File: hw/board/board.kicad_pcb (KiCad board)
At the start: 4 copper layers, 100 x 85 mm, 77 parts, among them J1 Conn_ARM_JTAG_SWD_10, J2 Conn_ARM_JTAG_SWD_10, SW1 TSB008A2526A, SW2 TSB008A2526A, U1 STM32F302CBTx, U2 W25Q128JVSIQTR, U3 AP7361C-18SP-13, U4 AP7361C-10E, U5 TPS54331DR, U6 XC7A35T-FTG256

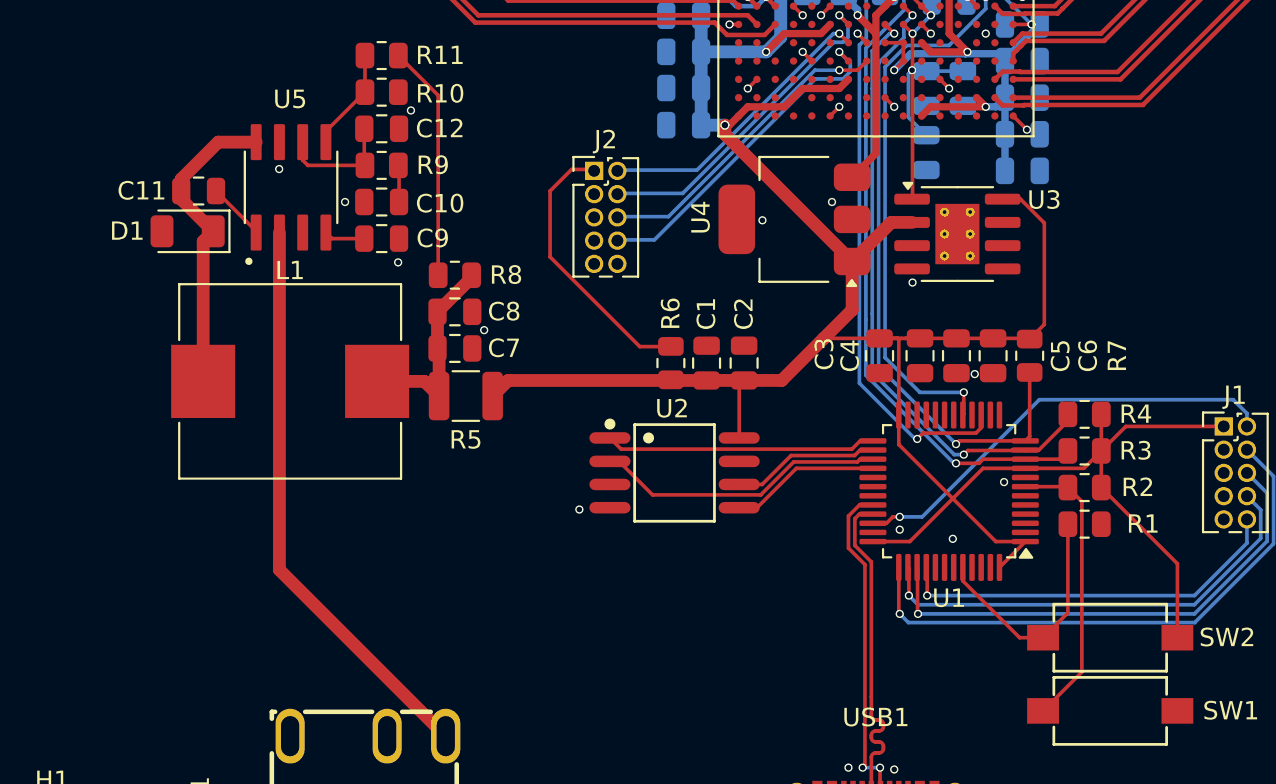
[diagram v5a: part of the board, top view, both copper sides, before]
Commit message: Added capacitor for STM32 NRST
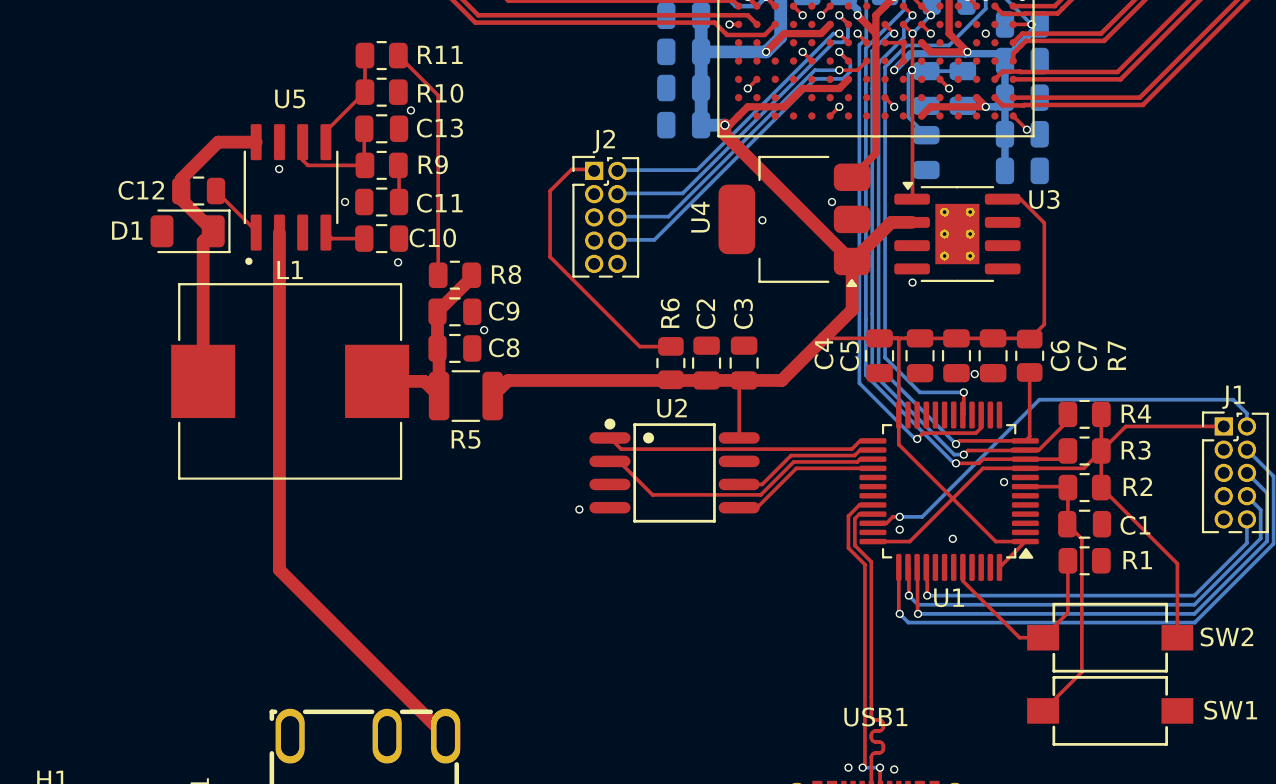
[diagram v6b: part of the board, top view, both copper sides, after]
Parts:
- added C1: 100n, Capacitor_SMD:C_0805_2012Metric, F.Cu at (145.4, 102.8)
- R1, R2: value 4k7 -> 10k
- moved R1 2.00 mm to (145.4, 104.8)
- renumbered C9 to C10, C10 to C11, C11 to C12, C12 to C13, C13 to C14, C14 to C15, C15 to C16, C16 to C17, C17 to C18, C18 to C19, C1 to C2, C19 to C20, C20 to C21, C21 to C22, C22 to C23, C23 to C24, C24 to C25, C25 to C26, C26 to C27, C27 to C28, C28 to C29, C2 to C3, C29 to C30, C30 to C31, C31 to C32, C32 to C33, C33 to C34, C34 to C35, C35 to C36, C36 to C37, C37 to C38, C38 to C39, C3 to C4, C39 to C40, C40 to C41, C4 to C5, C5 to C6, C6 to C7, C7 to C8, C8 to C9
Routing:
- net Net-(U1-BOOT0): track 13.2 -> 11.2 mm

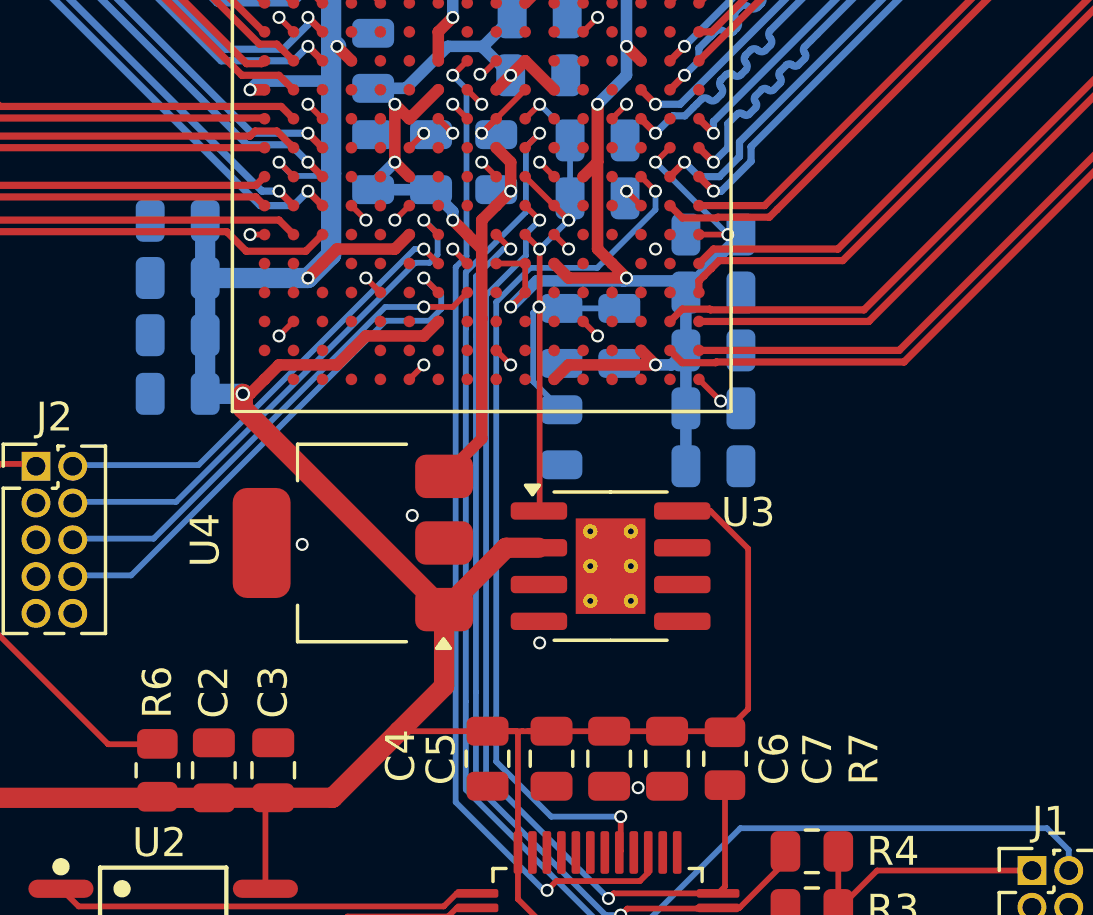
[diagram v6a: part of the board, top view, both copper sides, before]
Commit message: Moved linear regulators away from FPGA
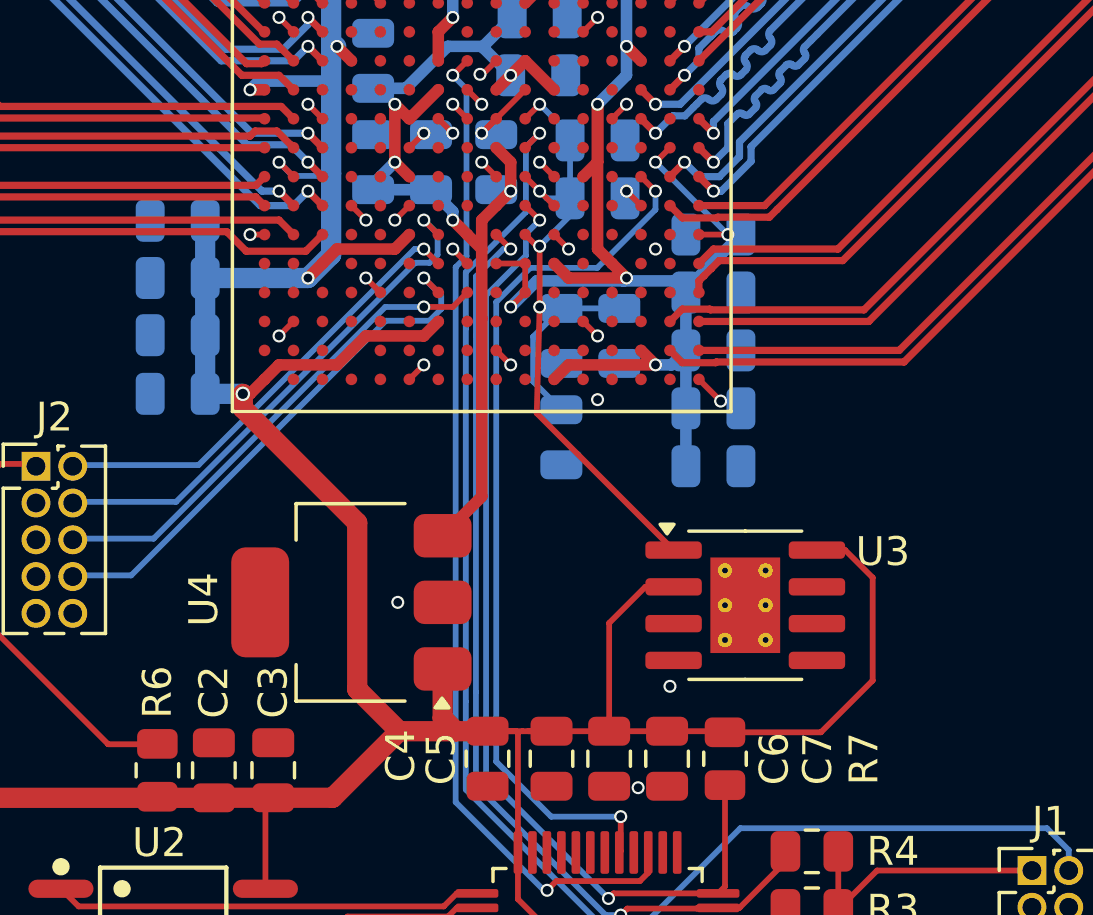
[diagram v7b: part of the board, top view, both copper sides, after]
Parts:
- moved U3 4.84 mm to (143.1, 88.3)
- moved U4 2.05 mm to (129.5, 88.2)
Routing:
- net +2V5: track 236.7 -> 241.6 mm
- net +1V8: track 25.9 -> 28.5 mm
- net +1V0: track 36.7 -> 38.7 mm

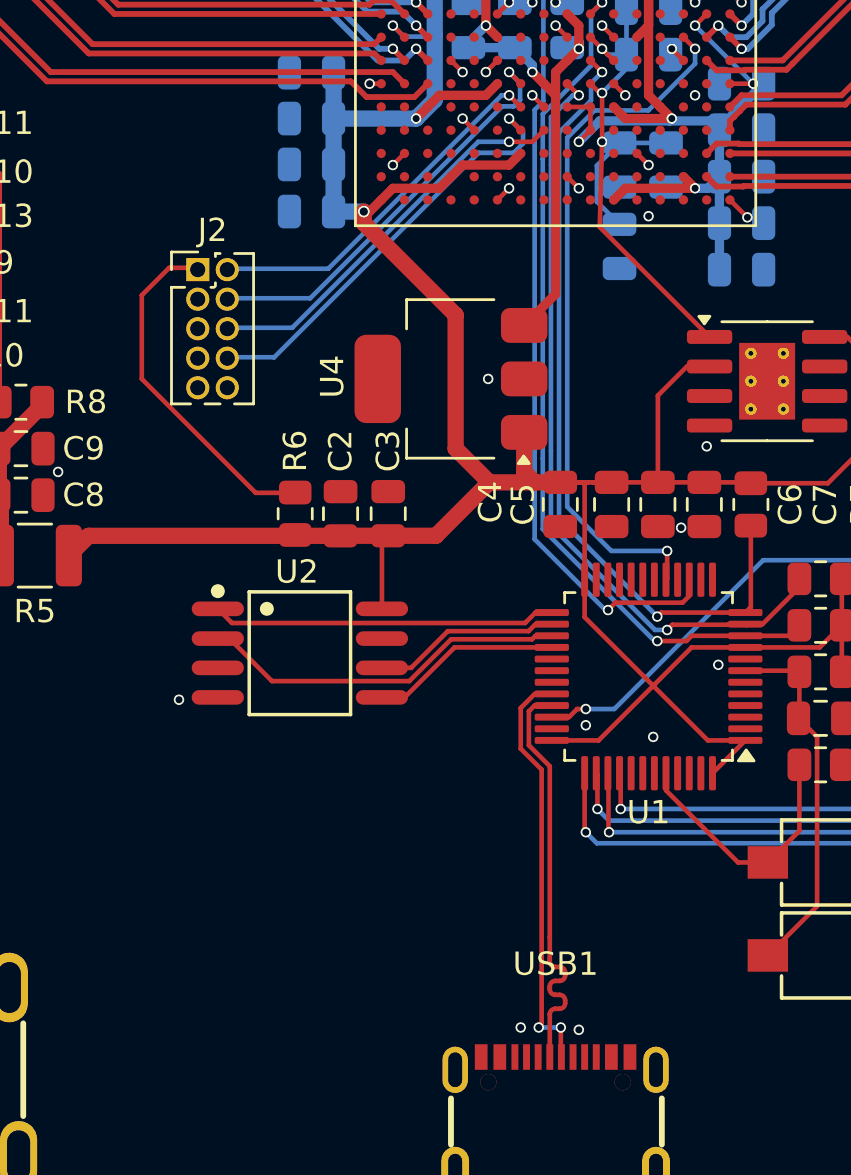
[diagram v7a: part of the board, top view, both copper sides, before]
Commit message: Cleaned up footprint placement, started BOM
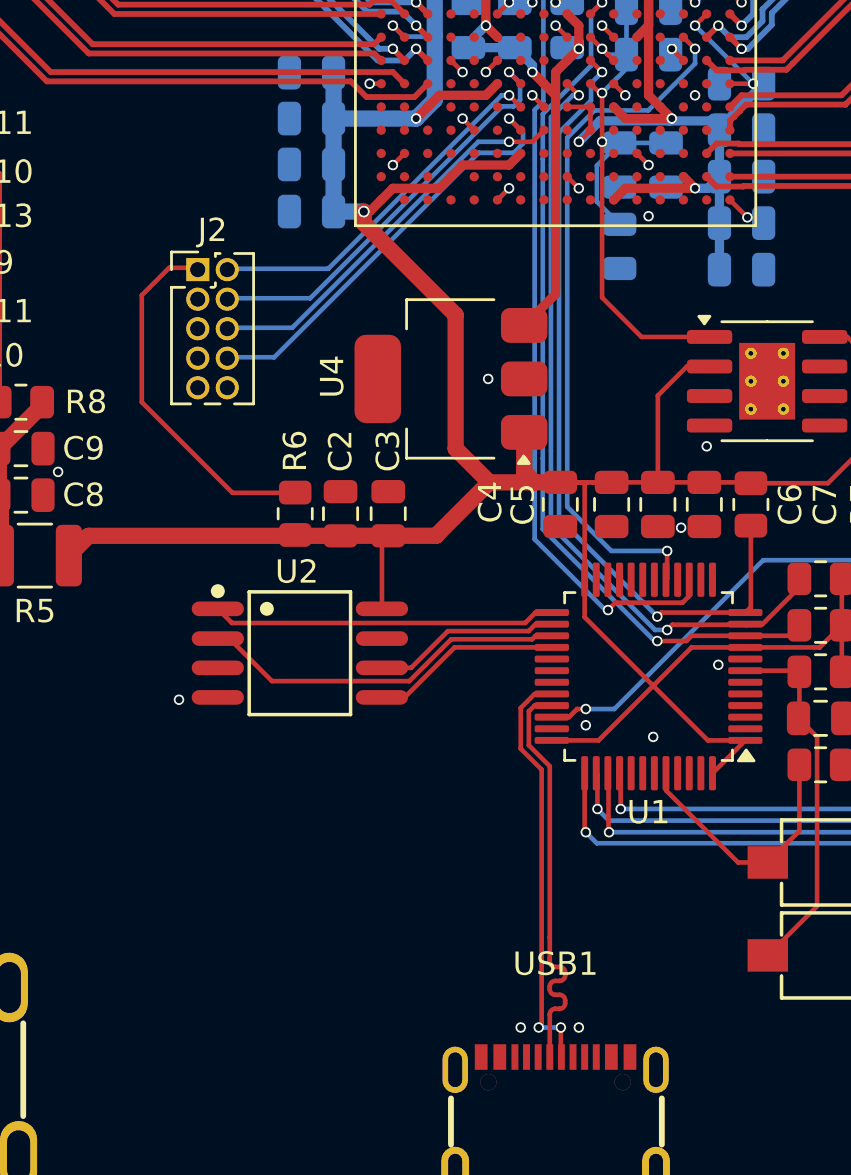
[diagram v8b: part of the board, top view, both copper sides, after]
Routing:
- net +1V8: track 28.5 -> 30.1 mm
- net Net-(J2-VTref): track 15.0 -> 15.6 mm
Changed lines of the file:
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@@
 	)
 	(net 0 "")
-	(net 1 "Net-(C7-Pad1)")
+	(net 1 "Net-(C8-Pad1)")
 	(net 2 "D_{out}4_P")
 	(net 3 "S_{in}1_P")
@@
 	(net 11 "PROGRAM_B")
 	(net 12 "D_{out}4_N")
-	(net 13 "Net-(C10-Pad1)")
+	(net 13 "Net-(C11-Pad1)")
 	(net 14 "Net-(U5-BOOT)")
 	(net 15 "D_{in}1_N")
@@
 			(layers "F.Cu" "F.Paste" "F.Mask")
 			(roundrect_rratio 0.25)
-			(net 1 "Net-(C7-Pad1)")
+			(net 1 "Net-(C8-Pad1)")
 			(pintype "passive")
 		)
@@
 			(layers "F.Cu" "F.Paste" "F.Mask")
 			(roundrect_rratio 0.222222)
-			(net 1 "Net-(C7-Pad1)")
+			(net 1 "Net-(C8-Pad1)")
 			(pintype "passive")
 		)
@@
 			(layers "F.Cu" "F.Paste" "F.Mask")
 			(roundrect_rratio 0.25)
-			(net 13 "Net-(C10-Pad1)")
+			(net 13 "Net-(C11-Pad1)")
 			(pintype "passive")
 		)
@@
 			(size 3.5 4)
 			(layers "F.Cu" "F.Paste" "F.Mask")
-			(net 1 "Net-(C7-Pad1)")
+			(net 1 "Net-(C8-Pad1)")
 			(pinfunction "2")
 			(pintype "passive")
@@
 			(layers "F.Cu" "F.Paste" "F.Mask")
 			(roundrect_rratio 0.243902)
-			(net 1 "Net-(C7-Pad1)")
+			(net 1 "Net-(C8-Pad1)")
 			(pintype "passive")
 		)
@@
 			(layers "F.Cu" "F.Paste" "F.Mask")
 			(roundrect_rratio 0.25)
-			(net 1 "Net-(C7-Pad1)")
+			(net 1 "Net-(C8-Pad1)")
 			(pintype "passive")
 		)
@@
 			(layers "F.Cu" "F.Paste" "F.Mask")
 			(roundrect_rratio 0.243902)
-			(net 13 "Net-(C10-Pad1)")
+			(net 13 "Net-(C11-Pad1)")
 			(pintype "passive")
 		)
@@
 	)
 	(via
-		(at 135 116.2)
+		(at 135 116.1)
 		(size 0.45)
 		(drill 0.3)
@@
 	)
 	(segment
-		(start 136 74)
-		(end 136.5 74.5)
+		(start 137.695 86.395)
+		(end 136 84.7)
 		(width 0.2)
 		(layer "F.Cu")
@@
 	)
 	(segment
-		(start 135.5 71.5)
-		(end 136 71)
+		(start 136 84.7)
+		(end 136 78)
 		(width 0.2)
 		(layer "F.Cu")
@@
 	)
 	(segment
-		(start 136 75.9)
-		(end 135.9 75.9)
+		(start 136 74)
+		(end 136.5 74.5)
+		(width 0.2)
+		(layer "F.Cu")
+		(net 7)
+	)
+	(segment
+		(start 135.5 71.5)
+		(end 136 71)
 		(width 0.2)
 		(layer "F.Cu")
@@
 	(segment
 		(start 140.625 86.395)
-		(end 135.9 81.67)
+		(end 137.695 86.395)
 		(width 0.2)
 		(layer "F.Cu")
@@
 	)
 	(segment
-		(start 135.9 81.67)
-		(end 136 78)
+		(start 136 75.9)
+		(end 135.9 75.9)
 		(width 0.2)
 		(layer "F.Cu")
@@
 	)
 	(segment
-		(start 122.8 93.1)
-		(end 121.1 93.1)
+		(start 117.38 83.42)
+		(end 118.53 83.42)
 		(width 0.2)
 		(layer "F.Cu")
@@
 	)
 	(segment
-		(start 116.2 84.6)
-		(end 117.38 83.42)
+		(start 116.2 89.2)
+		(end 116.2 84.6)
 		(width 0.2)
 		(layer "F.Cu")
@@
 	)
 	(segment
-		(start 116.2 88.2)
-		(end 116.2 84.6)
+		(start 120.1 93.1)
+		(end 116.2 89.2)
 		(width 0.2)
 		(layer "F.Cu")
@@
 	)
 	(segment
-		(start 121.1 93.1)
-		(end 116.2 88.2)
+		(start 116.2 84.6)
+		(end 117.38 83.42)
 		(width 0.2)
 		(layer "F.Cu")
@@
 	)
 	(segment
-		(start 117.38 83.42)
-		(end 118.53 83.42)
+		(start 122.8 93.1)
+		(end 120.1 93.1)
 		(width 0.2)
 		(layer "F.Cu")
